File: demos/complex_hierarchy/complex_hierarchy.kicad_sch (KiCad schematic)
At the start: 10 parts, among them P1 CONN_2, P2 CONN_2, U1 ICL7660, U2 78L05

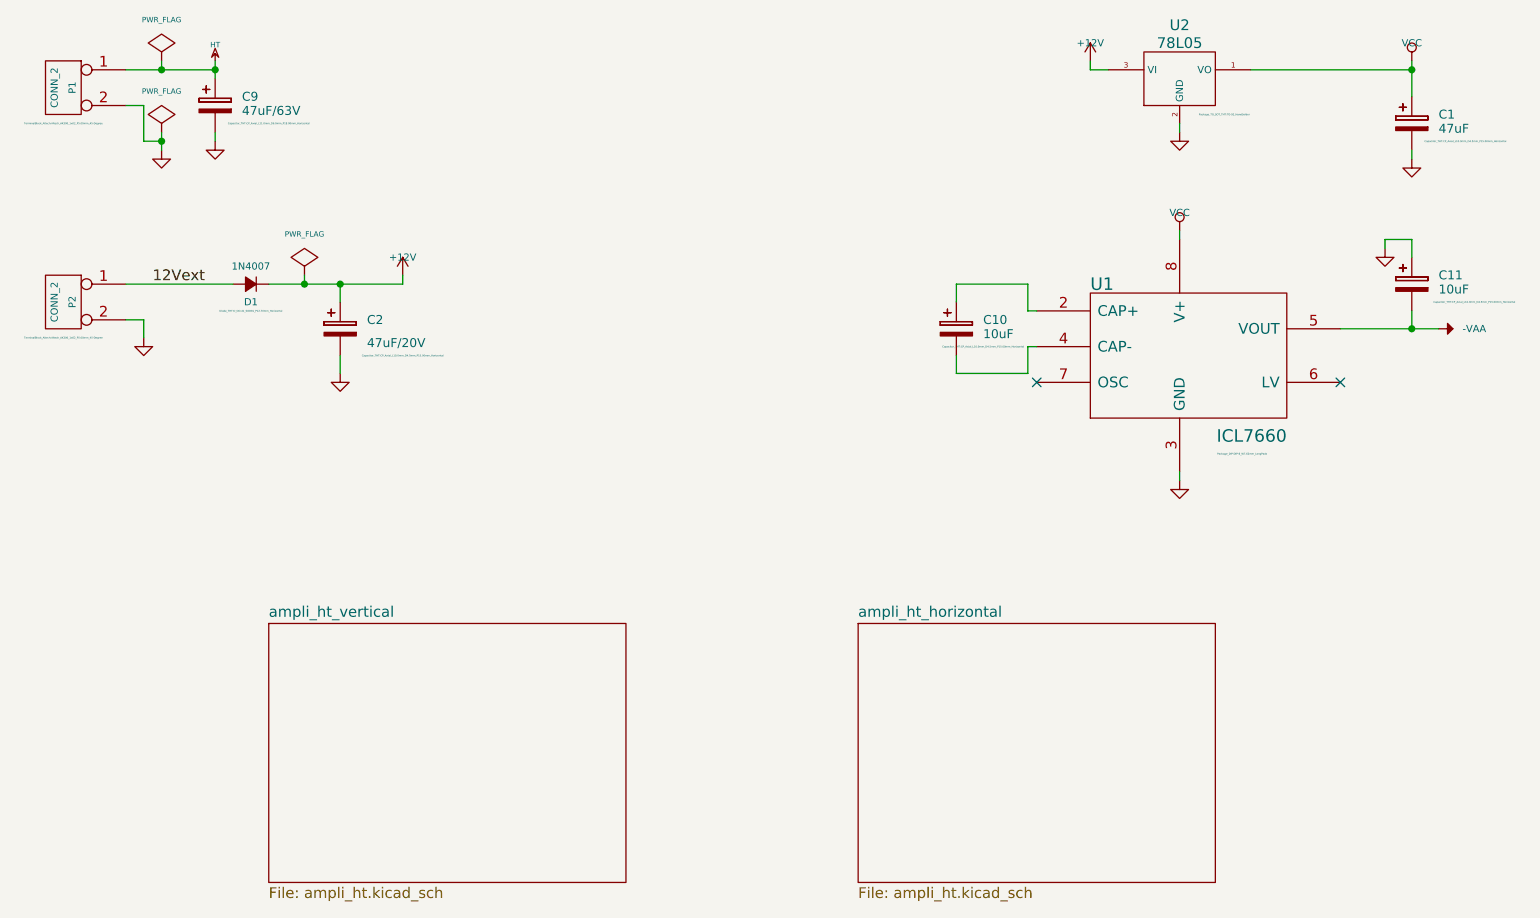
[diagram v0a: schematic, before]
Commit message: feat: update kicad to 9.0.0+dfsg-1
Signed-off-by: lhdjply <lhdjply@126.com>
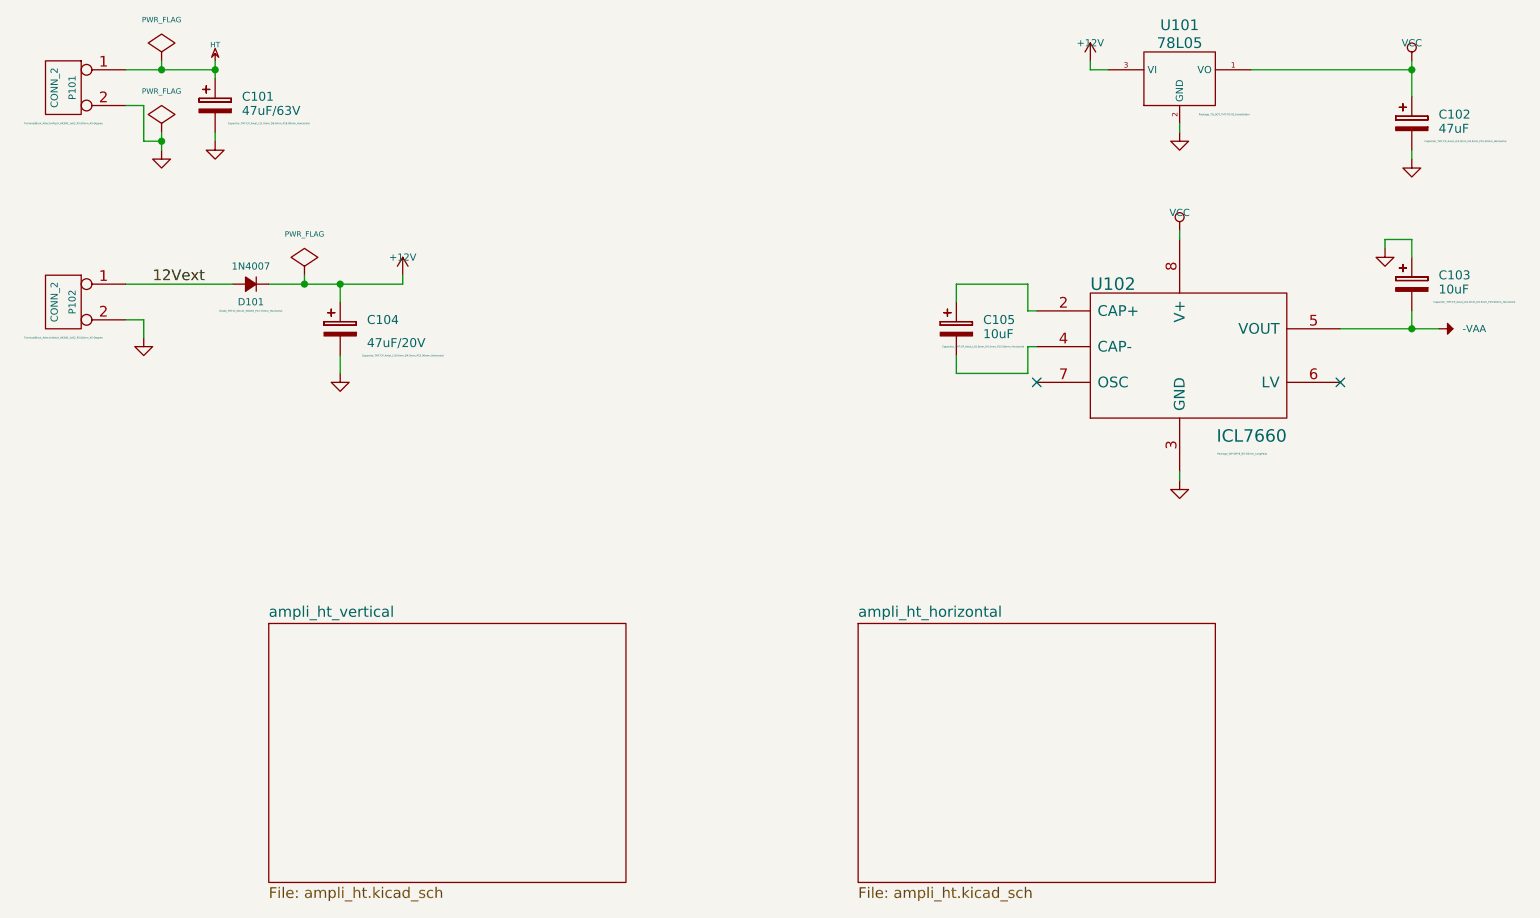
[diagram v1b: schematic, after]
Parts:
- C101: renamed from C9; symbol complex_hierarchy_schlib:CP -> complex_hierarchy:CP
- C102: renamed from C1; symbol complex_hierarchy_schlib:CP -> complex_hierarchy:CP
- C103: renamed from C11; symbol complex_hierarchy_schlib:CP -> complex_hierarchy:CP
- C104: renamed from C2; symbol complex_hierarchy_schlib:CP -> complex_hierarchy:CP
- C105: renamed from C10; symbol complex_hierarchy_schlib:CP -> complex_hierarchy:CP
- D101: renamed from D1; symbol complex_hierarchy_schlib:D_Small -> complex_hierarchy:D_Small
- P101: renamed from P1; symbol complex_hierarchy_schlib:CONN_2 -> complex_hierarchy:CONN_2
- P102: renamed from P2; symbol complex_hierarchy_schlib:CONN_2 -> complex_hierarchy:CONN_2
- U101: renamed from U2; symbol complex_hierarchy_schlib:7805 -> complex_hierarchy:7805
- U102: renamed from U1; symbol complex_hierarchy_schlib:ICL7660 -> complex_hierarchy:ICL7660
